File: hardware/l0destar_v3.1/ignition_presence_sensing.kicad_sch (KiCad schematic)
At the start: 5 parts

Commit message: update v3.1
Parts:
- S4R1: value 0402 120K 5% -> 0402 180K 5%
- S4R2: value 0402 100K 5% -> 0402 56K 5%
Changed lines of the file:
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@@
 			)
 		)
-		(property "Value" "0402 100K 5%"
+		(property "Value" "0402 56K 5%"
 			(at 46.99 63.5 0)
 			(show_name no)
@@
 			)
 		)
-		(property "Value" "0402 120K 5%"
+		(property "Value" "0402 180K 5%"
 			(at 55.88 49.53 90)
 			(show_name no)

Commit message: update v3.1
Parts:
- S4C1: Manufacturer_Name (none) -> Taiyo Yuden; Manufacturer_Part_Number (none) -> MCASU105SB7104KFNA01
- S4Q1: Manufacturer_Name (none) -> Multicomp Pro; Manufacturer_Part_Number (none) -> 2N7002
- S4R1: Manufacturer_Name (none) -> Multicomp Pro; Manufacturer_Part_Number (none) -> MCWR04X1803FTL
- S4R2, S4R3: Manufacturer_Name (none) -> Multicomp Pro; Manufacturer_Part_Number (none) -> MCMR04X5602FTL
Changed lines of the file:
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@@
 			)
 		)
-		(property "Datasheet" ""
+		(property "Datasheet" "https://uk.farnell.com/multicomp-pro/mcmr04x5602ftl/res-56k-1-0-0625w-0402-ceramic/dp/2073131"
 			(at 63.5 62.23 0)
 			(hide yes)
@@
 					(size 1.27 1.27)
 				)
+			)
+		)
+		(property "Manufacturer_Part_Number" "MCMR04X5602FTL"
+			(at 63.5 62.23 0)
+			(hide yes)
+			(show_name no)
+			(do_not_autoplace no)
+			(effects
+				(font
+					(size 1.27 1.27)
+				)
+				(justify left top)
+			)
+		)
+		(property "Manufacturer_Name" "Multicomp Pro"
+			(at 63.5 62.23 0)
+			(hide yes)
+			(show_name no)
+			(do_not_autoplace no)
+			(effects
+				(font
+					(size 1.27 1.27)
+				)
+				(justify left top)
 			)
 		)
@@
 			)
 		)
-		(property "Datasheet" ""
+		(property "Datasheet" "https://uk.farnell.com/multicomp-pro/mcmr04x5602ftl/res-56k-1-0-0625w-0402-ceramic/dp/2073131"
 			(at 72.39 38.1 0)
 			(hide yes)
@@
 					(size 1.27 1.27)
 				)
+			)
+		)
+		(property "Manufacturer_Part_Number" "MCMR04X5602FTL"
+			(at 72.39 38.1 0)
+			(hide yes)
+			(show_name no)
+			(do_not_autoplace no)
+			(effects
+				(font
+					(size 1.27 1.27)
+				)
+				(justify left top)
+			)
+		)
+		(property "Manufacturer_Name" "Multicomp Pro"
+			(at 72.39 38.1 0)
+			(hide yes)
+			(show_name no)
+			(do_not_autoplace no)
+			(effects
+				(font
+					(size 1.27 1.27)
+				)
+				(justify left top)
 			)
 		)
@@
 			)
 		)
-		(property "Datasheet" "https://www.onsemi.com/pub/Collateral/NDS7002A-D.PDF"
+		(property "Datasheet" "https://uk.farnell.com/multicomp-pro/2n7002/mosfet-n-ch-60v-0-115a-sot-23/dp/4295174"
 			(at 111.125 57.15 0)
 			(hide yes)
@@
 					(size 1.27 1.27)
 				)
+			)
+		)
+		(property "Manufacturer_Part_Number" "2N7002"
+			(at 111.125 57.15 0)
+			(hide yes)
+			(show_name no)
+			(do_not_autoplace no)
+			(effects
+				(font
+					(size 1.27 1.27)
+				)
+				(justify left top)
+			)
+		)
+		(property "Manufacturer_Name" "Multicomp Pro"
+			(at 111.125 57.15 0)
+			(hide yes)
+			(show_name no)
+			(do_not_autoplace no)
+			(effects
+				(font
+					(size 1.27 1.27)
+				)
+				(justify left top)
 			)
 		)
@@
 			)
 		)
-		(property "Datasheet" ""
+		(property "Datasheet" "https://uk.farnell.com/multicomp-pro/mcwr04x1803ftl/res-180k-1-0-0625w-thick-film/dp/2447116"
 			(at 55.88 53.34 0)
 			(hide yes)
@@
 					(size 1.27 1.27)
 				)
+			)
+		)
+		(property "Manufacturer_Part_Number" "MCWR04X1803FTL"
+			(at 55.88 53.34 0)
+			(hide yes)
+			(show_name no)
+			(do_not_autoplace no)
+			(effects
+				(font
+					(size 1.27 1.27)
+				)
+				(justify left top)
+			)
+		)
+		(property "Manufacturer_Name" "Multicomp Pro"
+			(at 55.88 53.34 0)
+			(hide yes)
+			(show_name no)
+			(do_not_autoplace no)
+			(effects
+				(font
+					(size 1.27 1.27)
+				)
+				(justify left top)
 			)
 		)
@@
 			)
 		)
-		(property "Datasheet" ""
+		(property "Datasheet" "https://ds.yuden.co.jp/TYCOMPAS/or/detail?pn=MCASU105SB7104KFNA01&u=M"
 			(at 76.2 62.23 0)
 			(hide yes)
@@
 			)
 		)
+		(property "Manufacturer_Part_Number" "MCASU105SB7104KFNA01"
+			(at 76.2 62.23 0)
+			(hide yes)
+			(show_name no)
+			(do_not_autoplace no)
+			(effects
+				(font
+					(size 1.27 1.27)
+				)
+				(justify left top)
+			)
+		)
+		(property "Manufacturer_Name" "Taiyo Yuden"
+			(at 76.2 62.23 0)
+			(hide yes)
+			(show_name no)
+			(do_not_autoplace no)
+			(effects
+				(font
+					(size 1.27 1.27)
+				)
+				(justify left top)
+			)
+		)

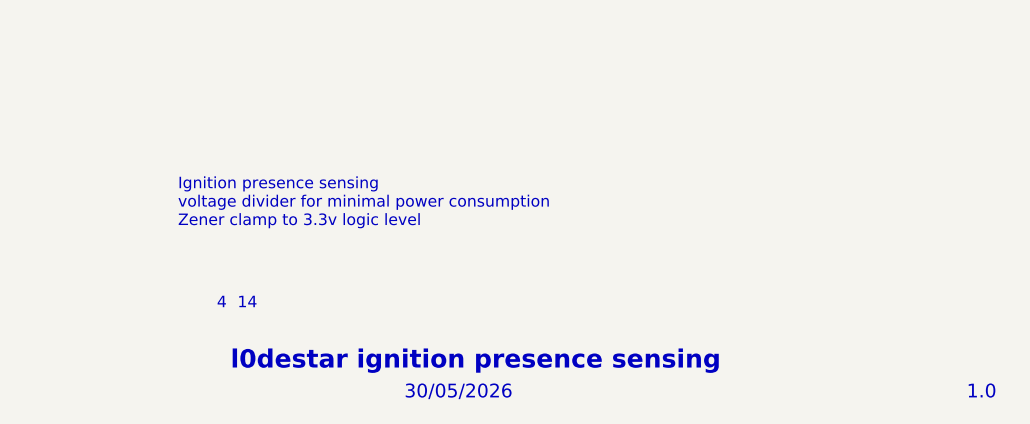
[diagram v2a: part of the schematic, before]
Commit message: update sheet annotations
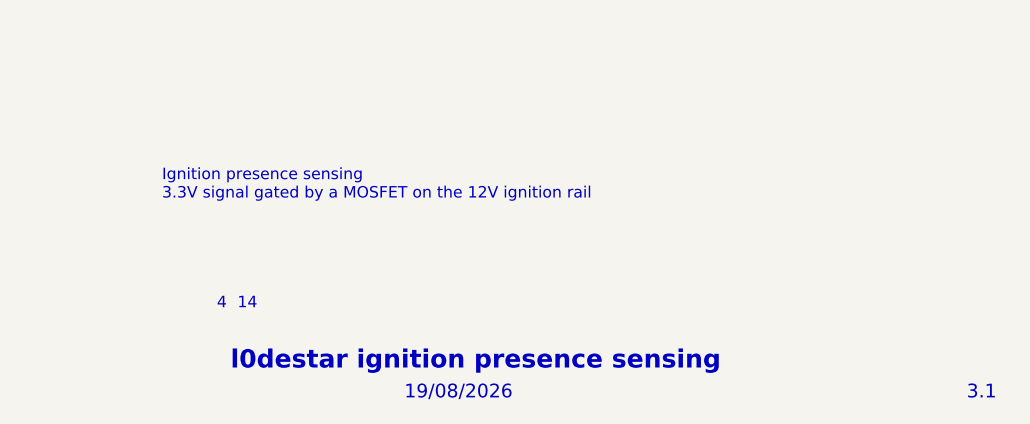
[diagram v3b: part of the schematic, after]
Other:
- note added: "19/08/2026"
- note added: "3.1"
- note added: "Ignition presence sensing 3.3V signal gated by a MOSFET on the 12V ignition rail"
- note removed: "1.0"
- note removed: "30/05/2026"
- note removed: "Ignition presence sensing voltage divider for minimal power consumption Zener clamp to 3.3v logic level"
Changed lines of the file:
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@@
 	(generator_version "10.0")
 	(paper "A4")
-	(text "1.0"
+	(text "3.1"
 		(exclude_from_sim no)
 		(at 268.478 193.294 0)
@@
 		)
 	)
-	(text "Ignition presence sensing\nvoltage divider for minimal power consumption\nZener clamp to 3.3v logic level"
+	(text "Ignition presence sensing\n3.3V signal gated by a MOSFET on the 12V ignition rail"
 		(exclude_from_sim no)
-		(at 180.848 172.212 0)
+		(at 179.07 170.18 0)
 		(effects
 			(font
@@
 		)
 	)
-	(text "30/05/2026"
+	(text "19/08/2026"
 		(exclude_from_sim no)
 		(at 205.994 193.294 0)

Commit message: schematic<>readme discrepency fixes
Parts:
- S4C1: Manufacturer_Name Taiyo Yuden -> Murata; Manufacturer_Part_Number MCASU105SB7104KFNA01 -> GRM155R71H104KE14D
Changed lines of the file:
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@@
 			)
 		)
-		(property "Datasheet" "https://ds.yuden.co.jp/TYCOMPAS/or/detail?pn=MCASU105SB7104KFNA01&u=M"
+		(property "Datasheet" ""
 			(at 76.2 62.23 0)
 			(hide yes)
@@
 			)
 		)
-		(property "Description" "Unpolarized capacitor"
+		(property "Description" ""
 			(at 76.2 62.23 0)
 			(hide yes)
@@
 			)
 		)
-		(property "Manufacturer_Part_Number" "MCASU105SB7104KFNA01"
+		(property "Manufacturer_Part_Number" "GRM155R71H104KE14D"
 			(at 76.2 62.23 0)
 			(hide yes)
@@
 			)
 		)
-		(property "Manufacturer_Name" "Taiyo Yuden"
+		(property "Manufacturer_Name" "Murata"
 			(at 76.2 62.23 0)
 			(hide yes)
